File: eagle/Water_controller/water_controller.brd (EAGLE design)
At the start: 152.4 x 88.9 mm, 50 parts, among them IC1 MAX3232CSE, J1 J12MM, J2 J12MM, J3 J12MM, Q1 IRF740, T1 BT138-V, T2 BT138-V, T3 BT138-V

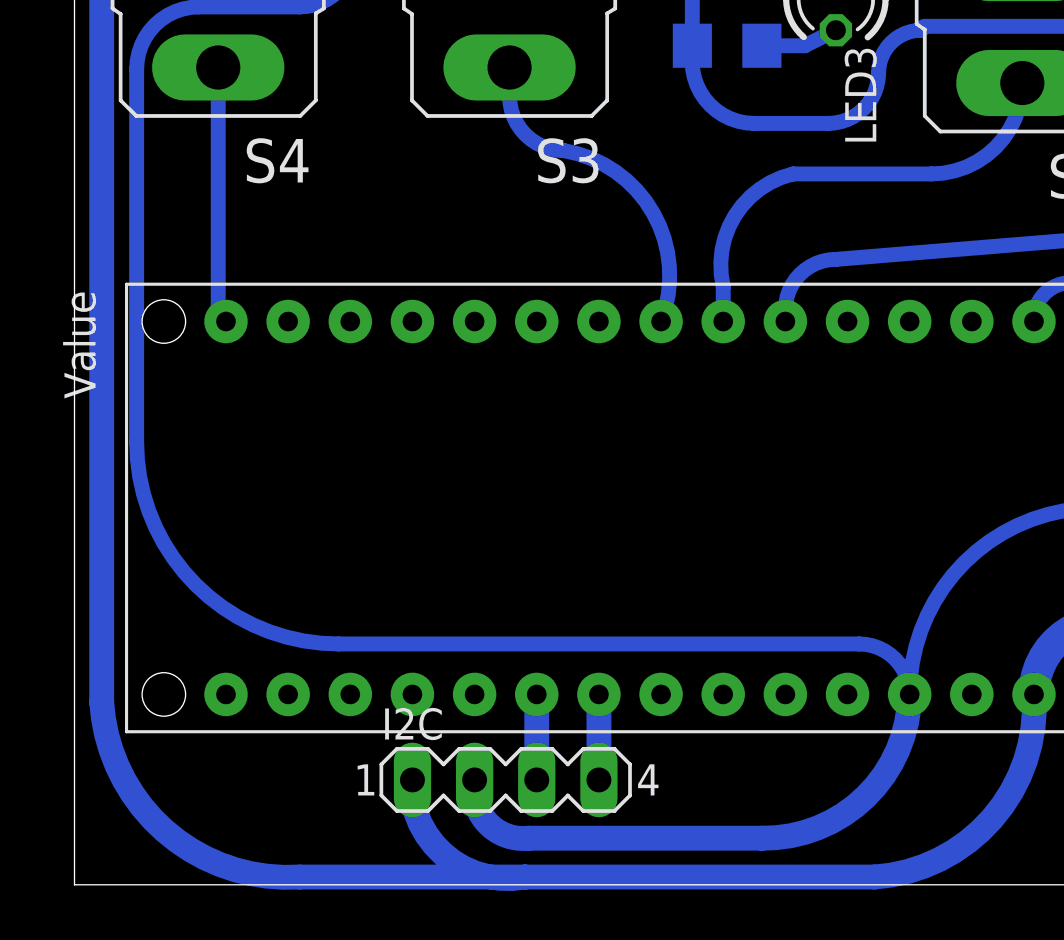
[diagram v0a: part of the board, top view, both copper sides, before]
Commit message: Defined two more time periods: medium and fast, set state machine to run in medium tome perod, and separated USART, statemachine and logging, such that they are indipendent and USART and logging are not called within the state machine. Muche feedback needed and ALL code so far 8)
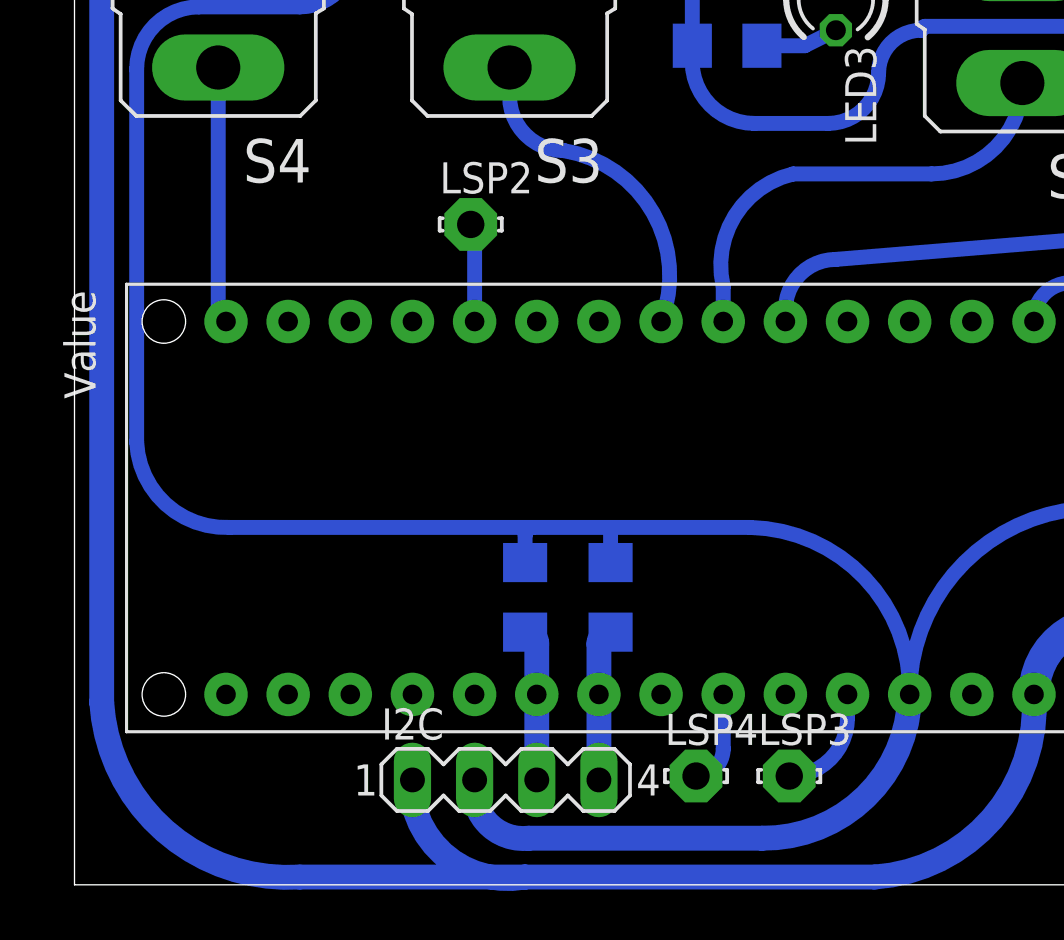
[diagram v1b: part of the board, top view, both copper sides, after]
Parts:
- added LSP2, LSP3, LSP4: LSP11, solpad:LSP11
- added R18, R20: 1.8k, resistor:R1206
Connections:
- new net N$33: LSP4.MP, U$1.A2
- new net N$34: LSP3.MP, U$1.A0
- net 5V: now also R18.1, R20.1
- net FREQ: now also LSP2.MP
- net SCL: now also R18.2
- net SDA: now also R20.2
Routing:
- net N$34: track 0.00 -> 4.32 mm
- net FREQ: track 0.00 -> 4.03 mm
- net N$33: track 0.00 -> 3.80 mm
- net 5V: track 184.4 -> 187.4 mm
- net SDA: track 3.49 -> 6.24 mm
- net SCL: track 3.49 -> 6.24 mm
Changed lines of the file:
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@@
 <element name="J2" library="jumper" package="12" value="J12MM" x="53.34" y="55.245" rot="R90"/>
 <element name="J3" library="jumper" package="12" value="J12MM" x="33.02" y="55.245" rot="R90"/>
+<element name="R18" library="resistor" package="R1206" value="1.8k" x="18.415" y="11.7475" rot="MR270"/>
+<element name="R20" library="resistor" package="R1206" value="1.8k" x="21.9075" y="11.7475" rot="MR270"/>
+<element name="LSP2" library="solpad" package="LSP11" value="LSP11" x="16.1925" y="26.9875"/>
+<element name="LSP3" library="solpad" package="LSP11" value="LSP11" x="29.21" y="4.445"/>
+<element name="LSP4" library="solpad" package="LSP11" value="LSP11" x="25.4" y="4.445"/>
 </elements>
 <signals>
@@
 <wire x1="5.08" y1="35.8775" x2="2.54" y2="33.3375" width="0.6096" layer="16" curve="90"/>
 <wire x1="2.54" y1="33.3375" x2="2.54" y2="18.0975" width="0.6096" layer="16"/>
-<wire x1="2.54" y1="18.0975" x2="10.795" y2="9.8425" width="0.6096" layer="16" curve="90"/>
-<wire x1="10.795" y1="9.8425" x2="32.06875" y2="9.8425" width="0.6096" layer="16"/>
-<wire x1="32.06875" y1="9.8425" x2="34.13125" y2="7.78" width="0.6096" layer="16" curve="-90"/>
+<wire x1="2.54" y1="18.0975" x2="6.35" y2="14.605" width="0.6096" layer="16" curve="90"/>
+<wire x1="6.35" y1="14.605" x2="18.7325" y2="14.605" width="0.6096" layer="16"/>
+<wire x1="18.7325" y1="14.605" x2="21.9075" y2="14.605" width="0.6096" layer="16"/>
+<wire x1="21.9075" y1="14.605" x2="27.62375" y2="14.605" width="0.6096" layer="16"/>
+<wire x1="27.62375" y1="14.605" x2="34.13125" y2="7.78" width="0.6096" layer="16" curve="-90"/>
 <wire x1="5.87375" y1="42.799" x2="6.731" y2="42.799" width="0.6096" layer="16"/>
 <wire x1="6.731" y1="42.799" x2="11.43" y2="38.1" width="0.6096" layer="16" curve="-90"/>
@@
 <wire x1="38.735" y1="46.355" x2="56.515" y2="46.355" width="0.6096" layer="16"/>
 <wire x1="56.515" y1="46.355" x2="59.69" y2="43.18" width="0.6096" layer="16" curve="-90"/>
+<contactref element="R18" pad="1"/>
+<contactref element="R20" pad="1"/>
+<wire x1="18.415" y1="13.1695" x2="18.415" y2="14.2875" width="0.6096" layer="16"/>
+<wire x1="18.415" y1="14.2875" x2="18.7325" y2="14.605" width="0.6096" layer="16" curve="-90"/>
+<wire x1="21.9075" y1="13.1695" x2="21.9075" y2="14.605" width="0.6096" layer="16"/>
 </signal>
 <signal name="GND">
@@
 <contactref element="I2C" pad="4"/>
 <wire x1="21.43125" y1="4.28625" x2="21.43125" y2="7.78" width="1.016" layer="16"/>
+<contactref element="R20" pad="2"/>
+<wire x1="21.43125" y1="7.78" x2="21.43125" y2="9.84925" width="1.016" layer="16"/>
+<wire x1="21.43125" y1="9.84925" x2="21.9075" y2="10.3255" width="1.016" layer="16" curve="-90"/>
 </signal>
 <signal name="SCL">
@@
 <contactref element="I2C" pad="3"/>
 <wire x1="18.89125" y1="4.28625" x2="18.89125" y2="7.78" width="1.016" layer="16"/>
+<contactref element="R18" pad="2"/>
+<wire x1="18.89125" y1="7.78" x2="18.89125" y2="9.84925" width="1.016" layer="16"/>
+<wire x1="18.89125" y1="9.84925" x2="18.415" y2="10.3255" width="1.016" layer="16" curve="90"/>
 </signal>
 <signal name="FREQ">
 <contactref element="U$1" pad="D8"/>
+<contactref element="LSP2" pad="MP"/>
+<wire x1="16.35125" y1="23.02" x2="16.35125" y2="26.82875" width="0.6096" layer="16"/>
+<wire x1="16.35125" y1="26.82875" x2="16.1925" y2="26.9875" width="0.6096" layer="16" curve="90"/>
 </signal>
 <signal name="NEUTRAL">
@@
 <wire x1="57.4675" y1="18.57375" x2="57.4675" y2="17.83715" width="0.6096" layer="16"/>
 </signal>
+<signal name="N$34">
+<contactref element="U$1" pad="A0"/>
+<contactref element="LSP3" pad="MP"/>
+<wire x1="31.59125" y1="7.78" x2="31.59125" y2="6.82625" width="0.6096" layer="16"/>
+<wire x1="31.59125" y1="6.82625" x2="29.21" y2="4.445" width="0.6096" layer="16" curve="-90"/>
+</signal>
+<signal name="N$33">
+<contactref element="U$1" pad="A2"/>
+<contactref element="LSP4" pad="MP"/>
+<wire x1="26.51125" y1="7.78" x2="26.51125" y2="5.55625" width="0.6096" layer="16"/>
+<wire x1="26.51125" y1="5.55625" x2="25.4" y2="4.445" width="0.6096" layer="16" curve="-90"/>
+</signal>
 </signals>

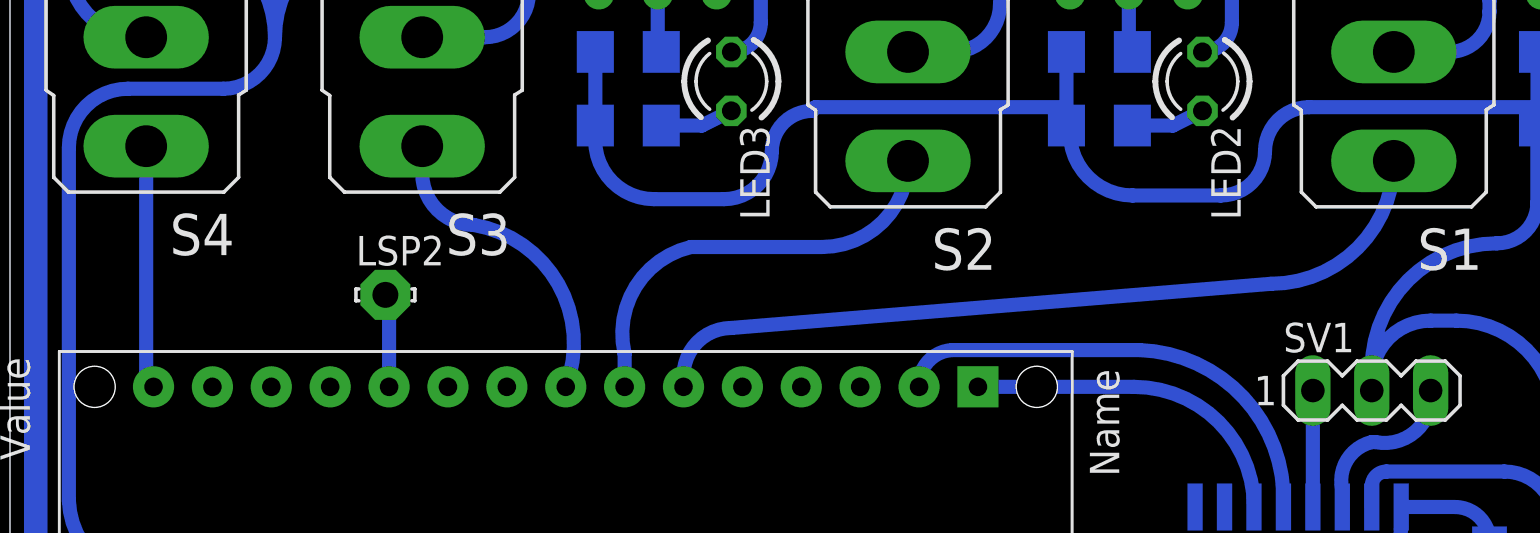
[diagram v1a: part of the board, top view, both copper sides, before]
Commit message: Wow, a Version 1.0alpha! Should be a working system _when_ program is populated with values... still to be done. Lots and lots to do... oh so much for a project that was supposed to take two weeks. Next step is splitting into separate projects, then EDAC, Web interface and daemon. Pretty happy with it thus far it has to be said. If only the hardware would stop loosing legs and being annoying. The breakout board is for a chip that is just too tiny for words. Enjoy and go hard. Please pay note to the the use of bitwise operations in the state machine and check. logical operators may be more efficient.
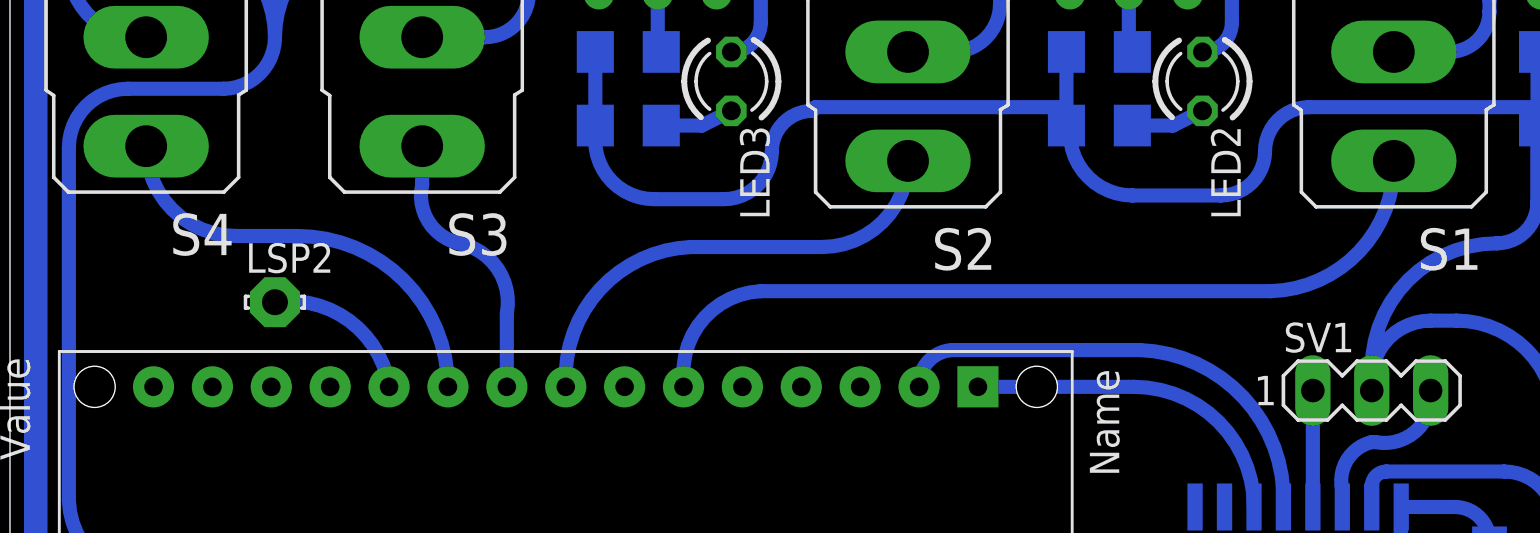
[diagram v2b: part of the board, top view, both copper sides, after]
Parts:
- moved LSP2 4.77 mm to (11.4, 26.7)
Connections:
- net FILL: now also U$1.D7; no longer U$1.D12
- net HEAT0: now also U$1.D5; no longer U$1.D4
- net HEAT1: now also U$1.D6; no longer U$1.D5
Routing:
- net FILL: track 10.5 -> 17.3 mm
- net FREQ: track 4.03 -> 6.13 mm
- net HEAT0: track 17.8 -> 18.9 mm
- net PUMP: track 34.2 -> 35.1 mm
- net HEAT1: track 12.4 -> 11.5 mm
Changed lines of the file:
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@@
 <element name="R18" library="resistor" package="R1206" value="1.8k" x="18.415" y="11.7475" rot="MR270"/>
 <element name="R20" library="resistor" package="R1206" value="1.8k" x="21.9075" y="11.7475" rot="MR270"/>
-<element name="LSP2" library="solpad" package="LSP11" value="LSP11" x="16.1925" y="26.9875"/>
+<element name="LSP2" library="solpad" package="LSP11" value="LSP11" x="11.43" y="26.67"/>
 <element name="LSP3" library="solpad" package="LSP11" value="LSP11" x="29.21" y="4.445"/>
 <element name="LSP4" library="solpad" package="LSP11" value="LSP11" x="25.4" y="4.445"/>
@@
 <signal name="HEAT1">
 <contactref element="S3" pad="1"/>
-<contactref element="U$1" pad="D5"/>
-<wire x1="17.78" y1="33.401" x2="17.78" y2="32.22625" width="0.6096" layer="16"/>
-<wire x1="17.78" y1="32.22625" x2="20.0025" y2="30.00375" width="0.6096" layer="16" curve="90"/>
-<wire x1="20.0025" y1="30.00375" x2="23.97125" y2="23.02" width="0.6096" layer="16" curve="-101.798483"/>
+<wire x1="19.3675" y1="29.21" x2="17.78" y2="31.75" width="0.6096" layer="16" curve="-90"/>
+<wire x1="17.78" y1="31.75" x2="17.78" y2="33.401" width="0.6096" layer="16"/>
+<contactref element="U$1" pad="D6"/>
+<wire x1="21.43125" y1="26.19375" x2="19.3675" y2="29.21" width="0.6096" layer="16" curve="90"/>
+<wire x1="21.43125" y1="26.19375" x2="21.43125" y2="23.02" width="0.6096" layer="16"/>
 </signal>
 <signal name="N$10">
@@
 <contactref element="U$1" pad="D3"/>
 <wire x1="29.05125" y1="23.02" x2="29.05125" y2="23.495" width="0.6096" layer="16"/>
-<wire x1="29.05125" y1="23.495" x2="31.115" y2="25.55875" width="0.6096" layer="16" curve="-90"/>
-<wire x1="31.115" y1="25.55875" x2="54.38775" y2="27.46375" width="0.6096" layer="16"/>
-<wire x1="54.38775" y1="27.46375" x2="59.69" y2="32.766" width="0.6096" layer="16" curve="90"/>
+<wire x1="29.05125" y1="23.495" x2="32.385" y2="27.14625" width="0.6096" layer="16" curve="-90"/>
+<wire x1="32.385" y1="27.14625" x2="54.38775" y2="27.14625" width="0.6096" layer="16"/>
+<wire x1="54.38775" y1="27.14625" x2="59.69" y2="32.766" width="0.6096" layer="16" curve="90"/>
 </signal>
 <signal name="HEAT0">
 <contactref element="S2" pad="1"/>
-<contactref element="U$1" pad="D4"/>
-<wire x1="26.51125" y1="23.02" x2="26.51125" y2="24.4475" width="0.6096" layer="16"/>
-<wire x1="26.51125" y1="24.4475" x2="29.36875" y2="29.05125" width="0.6096" layer="16" curve="-90"/>
+<wire x1="23.97125" y1="23.1775" x2="29.36875" y2="29.05125" width="0.6096" layer="16" curve="-90"/>
 <wire x1="29.36875" y1="29.05125" x2="35.02025" y2="29.05125" width="0.6096" layer="16"/>
 <wire x1="35.02025" y1="29.05125" x2="38.735" y2="32.766" width="0.6096" layer="16" curve="90"/>
+<contactref element="U$1" pad="D5"/>
+<wire x1="23.97125" y1="23.02" x2="23.97125" y2="23.1775" width="0" layer="19" extent="16-16"/>
 </signal>
 <signal name="P">
@@
 <signal name="FILL">
 <contactref element="S4" pad="1"/>
-<contactref element="U$1" pad="D12"/>
-<wire x1="5.87375" y1="33.401" x2="5.87375" y2="23.3375" width="0.6096" layer="16"/>
-<wire x1="5.87375" y1="23.3375" x2="6.19125" y2="23.02" width="0.6096" layer="16"/>
+<contactref element="U$1" pad="D7"/>
+<wire x1="18.89125" y1="23.02" x2="12.38375" y2="29.5275" width="0.6096" layer="16" curve="90"/>
+<wire x1="12.38375" y1="29.5275" x2="9.74725" y2="29.5275" width="0.6096" layer="16"/>
+<wire x1="9.74725" y1="29.5275" x2="5.87375" y2="33.401" width="0.6096" layer="16" curve="-90"/>
 </signal>
 <signal name="N$5">
@@
 <contactref element="U$1" pad="D8"/>
 <contactref element="LSP2" pad="MP"/>
-<wire x1="16.35125" y1="23.02" x2="16.35125" y2="26.82875" width="0.6096" layer="16"/>
-<wire x1="16.35125" y1="26.82875" x2="16.1925" y2="26.9875" width="0.6096" layer="16" curve="90"/>
+<wire x1="16.35125" y1="23.02" x2="16.35125" y2="23.01875" width="0.6096" layer="16"/>
+<wire x1="16.35125" y1="23.01875" x2="11.43" y2="26.67" width="0.6096" layer="16" curve="90"/>
 </signal>
 <signal name="NEUTRAL">
